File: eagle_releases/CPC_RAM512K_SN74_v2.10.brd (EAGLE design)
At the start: 90.2 x 81.3 mm, 19 parts

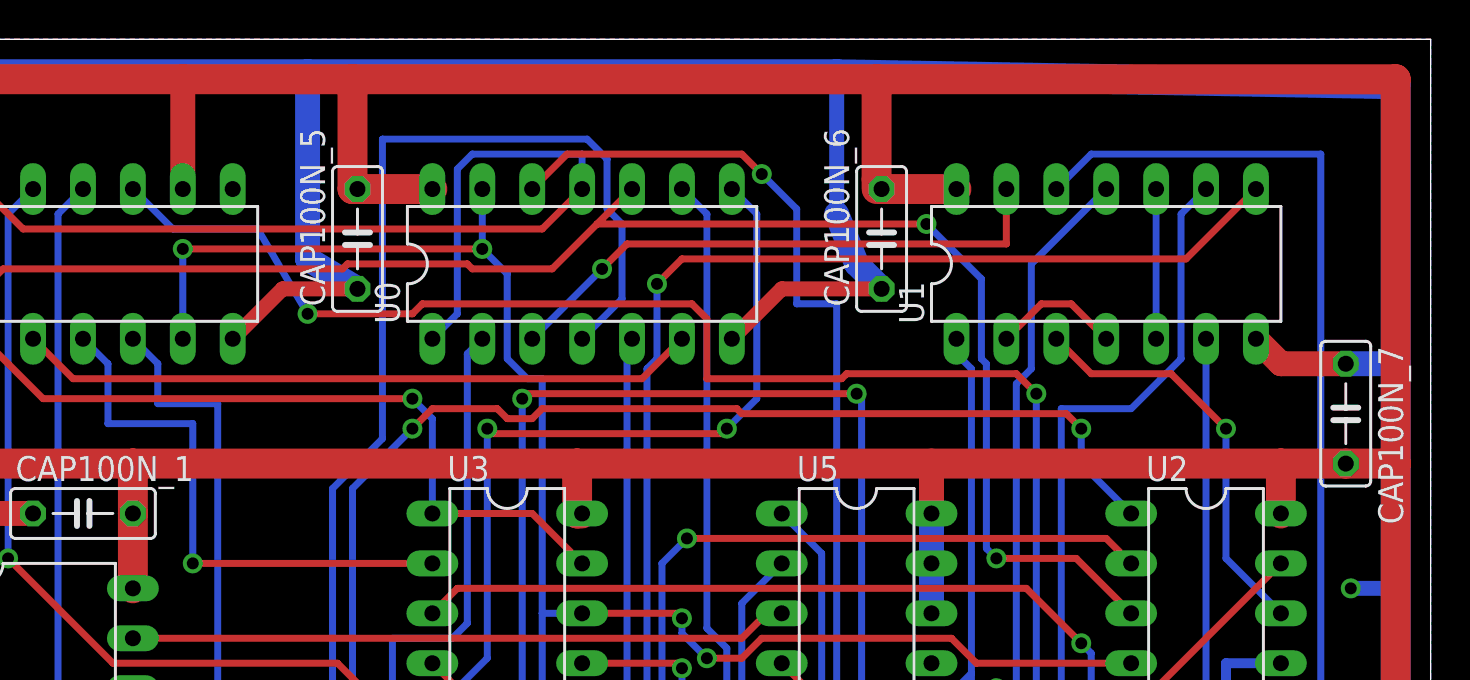
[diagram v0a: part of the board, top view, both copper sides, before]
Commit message: Add one more decap, minor power changes
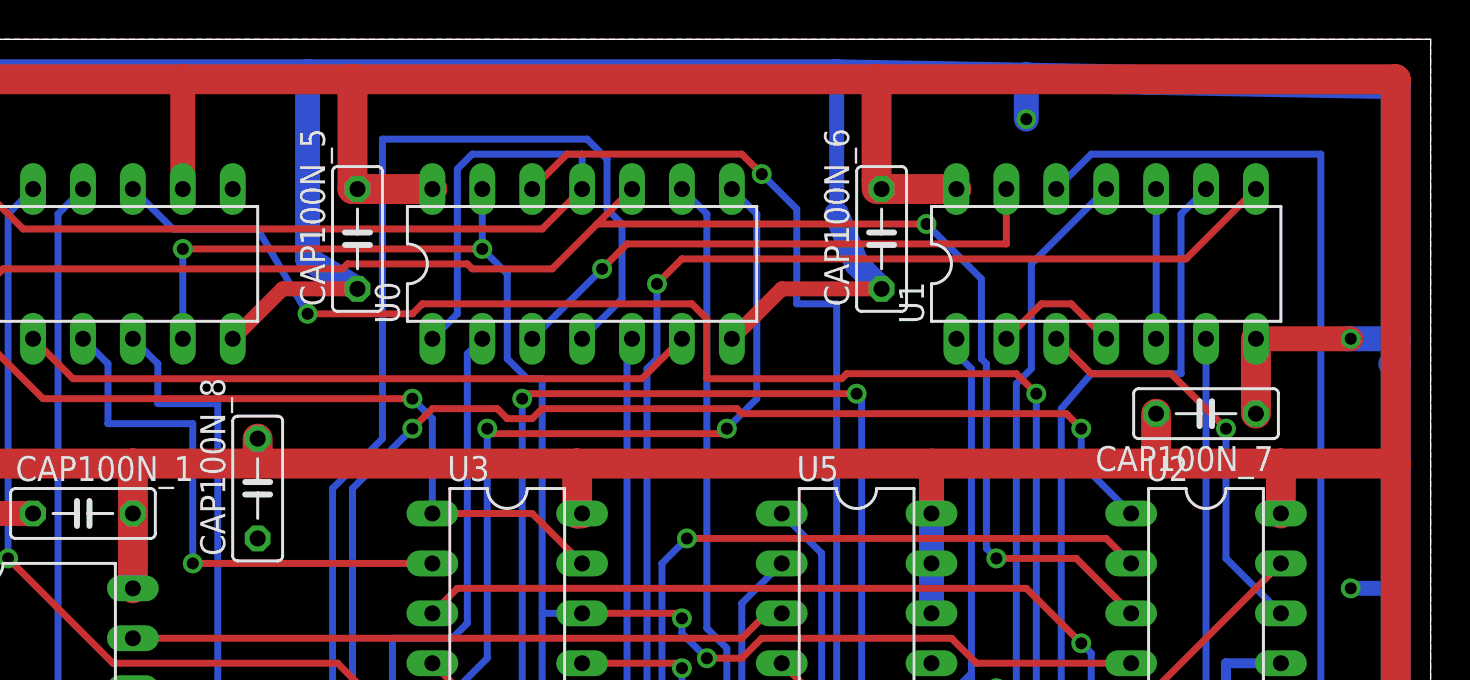
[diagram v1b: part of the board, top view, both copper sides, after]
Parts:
- added CAP100N_8: (no value), resistor:C050-025X075
- moved CAP100N_7 7.11 mm to (78.7, 62.2), turned to 180 degrees
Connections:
- net VDD: now also CAP100N_8.2
- net VSS: now also CAP100N_8.1
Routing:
- net VSS: track 576.8 -> 583.4 mm, vias 9 -> 11
- net VDD: track 545.7 -> 549.5 mm
- net RAMBLOCK_Q2: track 155.4 -> 155.9 mm
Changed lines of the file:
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@@
 <element name="CAP100N_5" library="resistor" package="C050-025X075" value="" x="35.56" y="71.12" rot="R90"/>
 <element name="CAP100N_6" library="resistor" package="C050-025X075" value="" x="62.23" y="71.12" rot="R90"/>
-<element name="CAP100N_7" library="resistor" package="C050-025X075" value="" x="85.852" y="62.23" rot="R270"/>
+<element name="CAP100N_7" library="resistor" package="C050-025X075" value="" x="78.74" y="62.23" rot="R180"/>
+<element name="CAP100N_8" library="resistor" package="C050-025X075" value="" x="30.48" y="58.42" rot="R90"/>
 </elements>
 <signals>
@@
 <wire x1="35.052" y1="16.51" x2="35.052" y2="17.526" width="0.3556" layer="1"/>
 <wire x1="77.47" y1="72.39" x2="78.74" y2="73.66" width="0.3556" layer="16"/>
-<wire x1="77.47" y1="65.024" x2="77.47" y2="72.39" width="0.3556" layer="16"/>
-<wire x1="74.93" y1="62.484" x2="77.47" y2="65.024" width="0.3556" layer="16"/>
-<wire x1="71.374" y1="62.484" x2="74.93" y2="62.484" width="0.3556" layer="16"/>
+<wire x1="77.47" y1="64.262" x2="77.47" y2="72.39" width="0.3556" layer="16"/>
+<wire x1="72.898" y1="64.262" x2="77.47" y2="64.262" width="0.3556" layer="16"/>
+<wire x1="71.374" y1="62.484" x2="72.898" y2="64.262" width="0.3556" layer="16"/>
 <wire x1="71.374" y1="22.098" x2="71.374" y2="62.484" width="0.3556" layer="16"/>
 <wire x1="65.786" y1="16.51" x2="71.374" y2="22.098" width="0.3556" layer="1"/>
@@
 <wire x1="2.032" y1="76.2" x2="2.032" y2="2.032" width="1.524" layer="1"/>
 <wire x1="44.45" y1="5.08" x2="44.45" y2="2.032" width="1.524" layer="1"/>
-<wire x1="85.852" y1="59.69" x2="82.55" y2="59.69" width="1.524" layer="1"/>
-<wire x1="82.55" y1="59.69" x2="64.77" y2="59.69" width="1.524" layer="1"/>
+<wire x1="88.392" y1="59.69" x2="82.55" y2="59.69" width="1.524" layer="1"/>
+<wire x1="82.55" y1="59.69" x2="76.2" y2="59.69" width="1.524" layer="1"/>
+<wire x1="76.2" y1="59.69" x2="64.77" y2="59.69" width="1.524" layer="1"/>
 <wire x1="64.77" y1="59.69" x2="46.736" y2="59.69" width="1.524" layer="1"/>
-<wire x1="46.736" y1="59.69" x2="24.13" y2="59.69" width="1.524" layer="1"/>
+<wire x1="46.736" y1="59.69" x2="30.48" y2="59.69" width="1.524" layer="1"/>
+<wire x1="30.48" y1="59.69" x2="24.13" y2="59.69" width="1.524" layer="1"/>
 <wire x1="24.13" y1="59.69" x2="24.13" y2="57.15" width="1.524" layer="1"/>
 <wire x1="24.13" y1="53.34" x2="24.13" y2="57.15" width="1.524" layer="1"/>
-<wire x1="85.852" y1="59.69" x2="88.392" y2="59.69" width="1.524" layer="1"/>
+<wire x1="76.2" y1="62.23" x2="76.2" y2="59.69" width="1.524" layer="1"/>
 <wire x1="82.55" y1="57.15" x2="82.55" y2="59.69" width="1.524" layer="1"/>
 <wire x1="46.99" y1="57.15" x2="46.736" y2="57.15" width="1.524" layer="1"/>
@@
 <contactref element="CAP22UF" pad="+"/>
 <wire x1="2.032" y1="76.2" x2="5.08" y2="76.2" width="1.27" layer="1"/>
+<contactref element="CAP100N_8" pad="2"/>
+<wire x1="30.48" y1="60.96" x2="30.48" y2="59.69" width="1.524" layer="1"/>
 </signal>
 <signal name="N28">
@@
 <contactref element="CONN1" pad="2"/>
 <contactref element="U0" pad="7"/>
-<contactref element="U1" pad="7"/>
 <contactref element="U2" pad="7"/>
 <contactref element="U3" pad="7"/>
@@
 <contactref element="CAP100N_5" pad="1"/>
 <contactref element="CAP100N_6" pad="1"/>
-<contactref element="CAP100N_7" pad="1"/>
 <wire x1="72.39" y1="5.08" x2="88.392" y2="5.08" width="1.524" layer="16"/>
 <wire x1="88.392" y1="5.08" x2="88.392" y2="37.084" width="1.524" layer="16"/>
 <wire x1="88.392" y1="37.084" x2="88.392" y2="64.77" width="1.524" layer="16"/>
-<wire x1="88.392" y1="64.77" x2="88.392" y2="78.994" width="1.524" layer="16"/>
+<wire x1="88.392" y1="64.77" x2="88.392" y2="66.04" width="1.524" layer="16"/>
+<wire x1="88.392" y1="66.04" x2="88.392" y2="78.994" width="1.524" layer="16"/>
 <wire x1="88.392" y1="78.994" x2="59.944" y2="79.502" width="1.524" layer="16"/>
 <wire x1="59.944" y1="79.502" x2="33.02" y2="79.502" width="1.524" layer="16"/>
@@
 <wire x1="72.39" y1="5.08" x2="78.486" y2="5.08" width="0.762" layer="1"/>
 <wire x1="88.392" y1="64.77" x2="88.138" y2="64.77" width="1.27" layer="16"/>
-<wire x1="88.138" y1="64.77" x2="85.852" y2="64.77" width="1.27" layer="16"/>
-<wire x1="82.55" y1="64.77" x2="81.28" y2="66.04" width="1.27" layer="1"/>
-<wire x1="85.852" y1="64.77" x2="82.55" y2="64.77" width="1.27" layer="1"/>
 <wire x1="33.02" y1="70.104" x2="35.56" y2="68.58" width="1.27" layer="16"/>
 <wire x1="33.02" y1="79.502" x2="33.02" y2="70.104" width="1.27" layer="16"/>
@@
 <wire x1="71.882" y1="4.826" x2="72.39" y2="5.08" width="0.762" layer="16"/>
 <via x="51.054" y="10.16" extent="1-16" drill="0.6096"/>
+<contactref element="CAP100N_8" pad="1"/>
+<wire x1="88.392" y1="66.04" x2="86.106" y2="66.04" width="1.27" layer="16"/>
+<contactref element="U1" pad="7"/>
+<contactref element="CAP100N_7" pad="1"/>
+<wire x1="86.106" y1="66.04" x2="85.852" y2="66.04" width="1.27" layer="16"/>
+<wire x1="81.28" y1="62.23" x2="81.28" y2="66.04" width="1.524" layer="1"/>
+<wire x1="81.28" y1="66.04" x2="86.106" y2="66.04" width="1.27" layer="1"/>
+<via x="86.106" y="66.04" extent="1-16" drill="0.6096"/>
+<wire x1="69.596" y1="79.502" x2="69.596" y2="77.216" width="1.27" layer="16"/>
+<via x="69.596" y="77.216" extent="1-16" drill="0.6096"/>
+<wire x1="81.28" y1="62.738" x2="81.28" y2="62.23" width="0.762" layer="16"/>
 </signal>
 <signal name="BUSACK_B">
